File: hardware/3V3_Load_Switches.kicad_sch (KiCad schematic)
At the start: 29 parts, among them Q18 SI2302DDS-T1-GE3, Q19 SI2302DDS-T1-GE3, Q20 SI2302DDS-T1-GE3, U1 LMV321RIYLT, U2 INA199C1DCKR, U3 INA199C1DCKR, U4 INA199C1DCKR, U5 NVTFS5116PLTAG, U6 NVTFS5116PLTAG, U7 NVTFS5116PLTAG

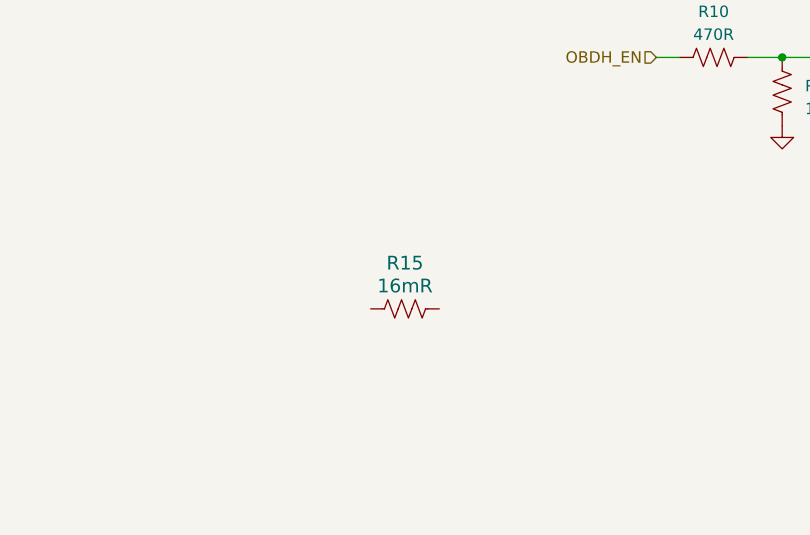
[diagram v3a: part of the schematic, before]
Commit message: hardware: update on footprints
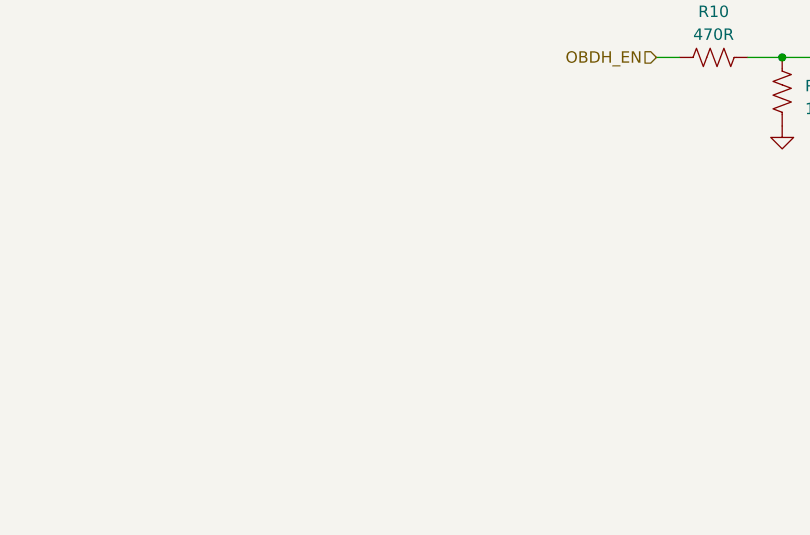
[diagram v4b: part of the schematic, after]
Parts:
- removed R15: 16mR, footprints:WSL2010R0330FEA, symbol WSL2010R0160FEA:WSL2010R0160FEA
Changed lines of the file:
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@@
-    )
-  )
-  (symbol (lib_id "WSL2010R0160FEA:WSL2010R0160FEA") (at 130.81 167.64 0) (unit 1)
-    (in_bom yes) (on_board yes) (dnp no) (fields_autoplaced)
-    (property "Reference" "R15" (at 137.16 162.56 0)
-      (effects (font (size 1.524 1.524)))
-    )
-    (property "Value" "16mR" (at 137.16 165.1 0)
-      (effects (font (size 1.524 1.524)))
-    )
-    (property "Footprint" "footprints:WSL2010R0330FEA" (at 134.62 177.8 0)
-      (effects (font (size 1.27 1.27) italic) hide)
-    )
-    (property "Datasheet" "WSL2010R0330FEA" (at 135.89 175.26 0)
-      (effects (font (size 1.27 1.27) italic) hide)
-    )
-    (pin "1")
-    (pin "2")
-    (instances
-      (project "eps-re_project"
-        (path "/2eebaa11-d7ed-4bfd-bc8e-988f68654d29/b2d6a676-b7d9-423e-8a54-05279452700b"
-          (reference "R15") (unit 1)
-        )
-      )
     )
   )

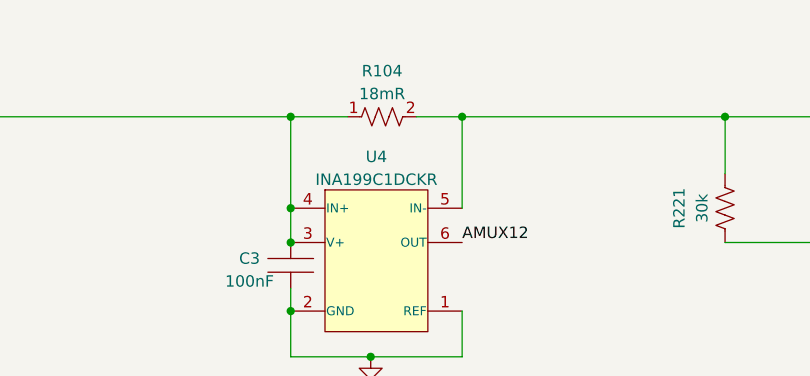
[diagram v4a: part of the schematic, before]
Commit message: hardware: all the resistors were validated, it is only missing the footprint and symbol of one MOSFET and other 4 components which i coulnd't found in the original project.
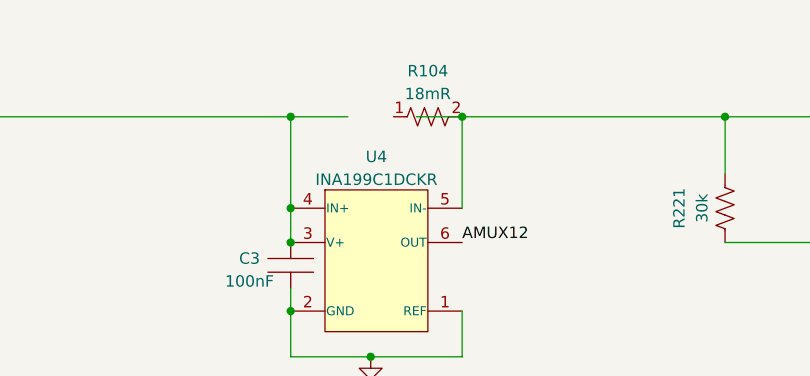
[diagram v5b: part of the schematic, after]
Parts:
- R104: footprint RESC5125X89N -> footprints:WSL2010R0180FEA
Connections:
- net +3V3: no longer R104.1
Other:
- moved on the sheet: R104
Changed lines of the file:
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@@
   (symbol (lib_id "WSL2010R0180FEA:WSL2010R0180FEA") (at 58.42 27.94 0) (unit 1)
     (in_bom yes) (on_board yes) (dnp no) (fields_autoplaced)
-    (property "Reference" "R104" (at 67.31 24.13 0)
-      (effects (font (size 1.27 1.27)))
-    )
-    (property "Value" "18mR" (at 67.31 26.67 0)
-      (effects (font (size 1.27 1.27)))
-    )
-    (property "Footprint" "RESC5125X89N" (at 72.39 124.13 0)
-      (effects (font (size 1.27 1.27)) (justify left top) hide)
-    )
-    (property "Datasheet" "https://www.arrow.com/en/products/wsl2010r0180fea/vishay" (at 72.39 224.13 0)
+    (property "Reference" "R104" (at 72.39 24.13 0)
+      (effects (font (size 1.27 1.27)))
+    )
+    (property "Value" "18mR" (at 72.39 26.67 0)
+      (effects (font (size 1.27 1.27)))
+    )
+    (property "Footprint" "footprints:WSL2010R0180FEA" (at 57.15 31.75 0)
+      (effects (font (size 1.27 1.27)) (justify left top) hide)
+    )
+    (property "Datasheet" "https://www.arrow.com/en/products/wsl2010r0180fea/vishay" (at 44.45 34.29 0)
       (effects (font (size 1.27 1.27)) (justify left top) hide)
     )
@@
       (effects (font (size 1.27 1.27) italic) hide)
     )
-    (property "Datasheet" "https://br.mouser.com/datasheet/2/308/1/NVTFS5116PL_D-2319932.pdf" (at 112.014 31.496 0)
+    (property "Datasheet" "https://br.mouser.com/datasheet/2/308/1/NVTFS5116PL_D-2319932.pdf" (at 111.76 31.75 0)
       (effects (font (size 1.27 1.27) italic) hide)
     )
@@
       (effects (font (size 1.27 1.27) italic) hide)
     )
-    (property "Datasheet" "https://br.mouser.com/datasheet/2/308/1/NVTFS5116PL_D-2319932.pdf" (at 112.014 117.856 0)
+    (property "Datasheet" "https://br.mouser.com/datasheet/2/308/1/NVTFS5116PL_D-2319932.pdf" (at 111.76 118.11 0)
       (effects (font (size 1.27 1.27) italic) hide)
     )
@@
       (effects (font (size 1.27 1.27) italic) hide)
     )
-    (property "Datasheet" "https://br.mouser.com/datasheet/2/308/1/NVTFS5116PL_D-2319932.pdf" (at 110.744 74.676 0)
+    (property "Datasheet" "https://br.mouser.com/datasheet/2/308/1/NVTFS5116PL_D-2319932.pdf" (at 110.49 74.93 0)
       (effects (font (size 1.27 1.27) italic) hide)
     )

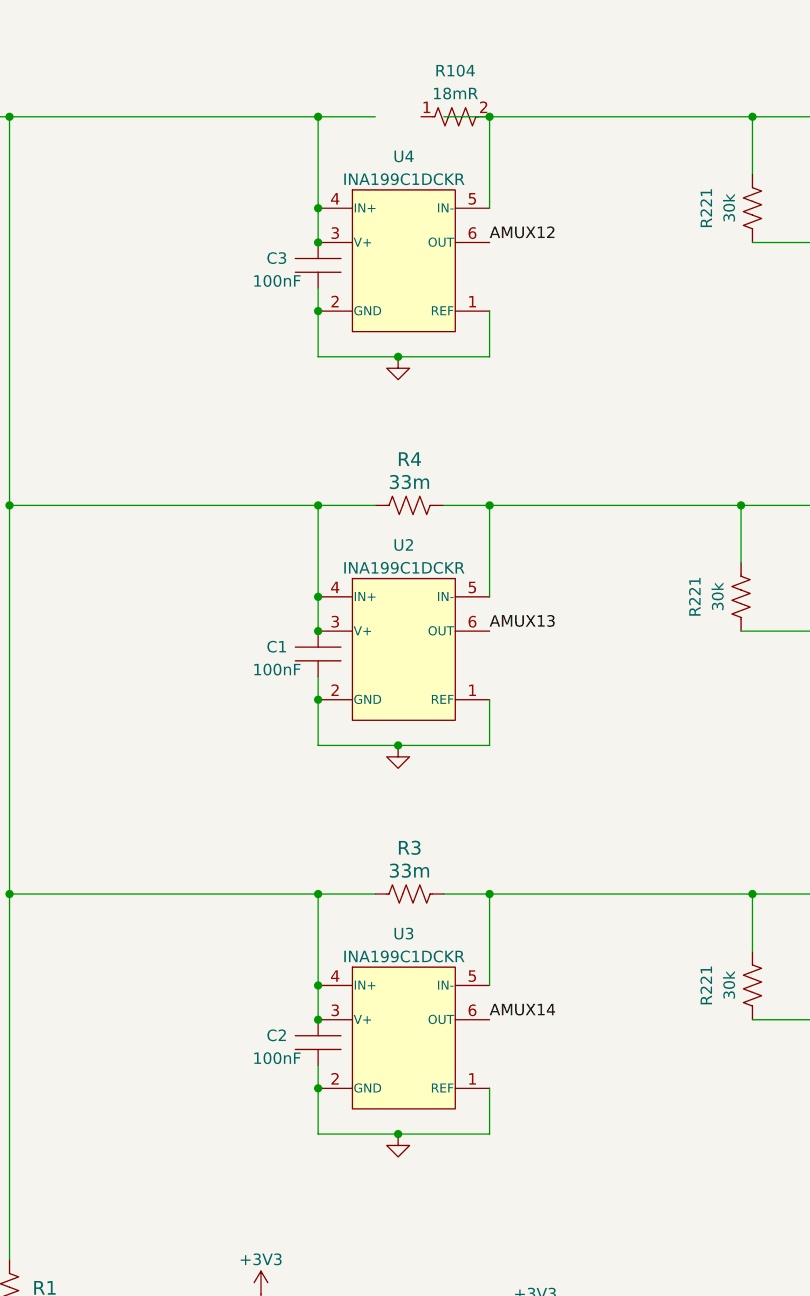
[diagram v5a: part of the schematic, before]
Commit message: hardware: Updating some footprints and 3D models.
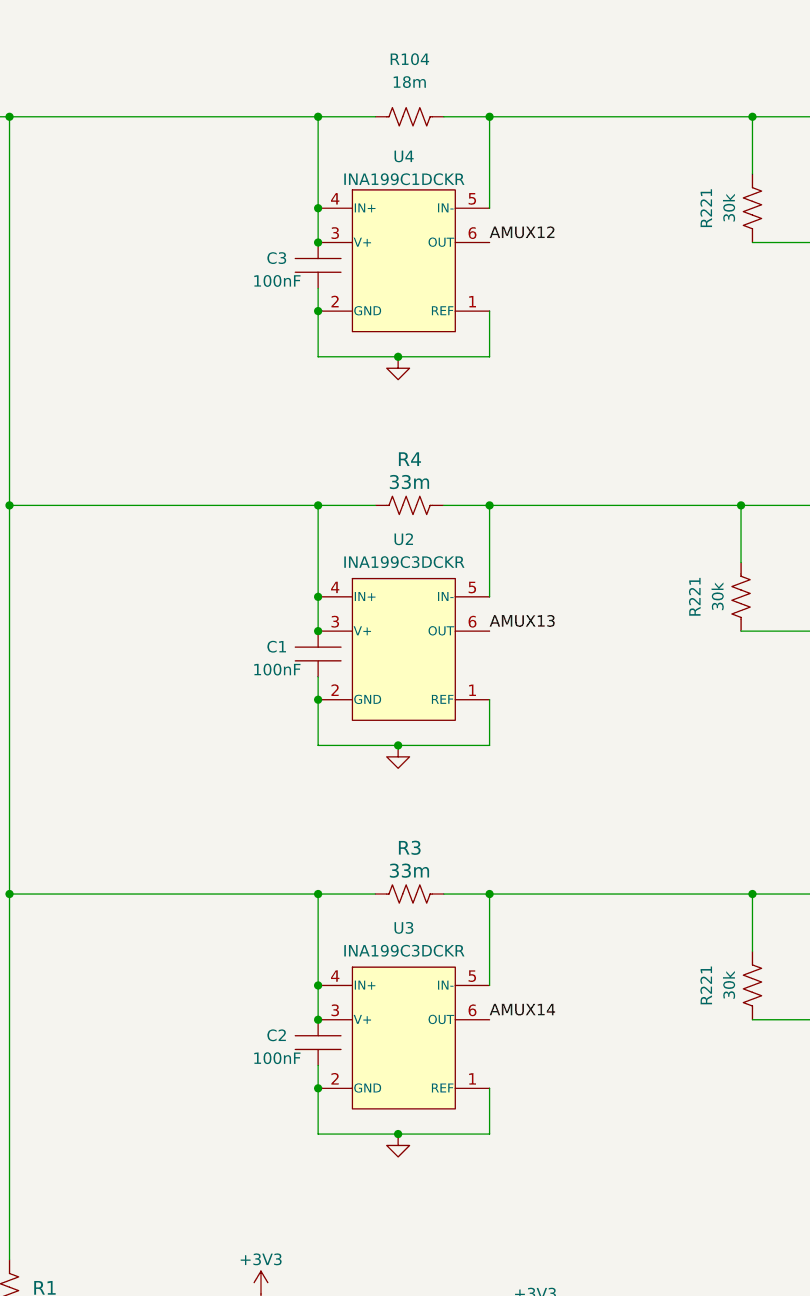
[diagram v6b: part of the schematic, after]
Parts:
- removed U2, U3: INA199C1DCKR, footprints:INA199C1DCKR, symbol INA199C1DCKR:INA199xxDCK
- added U2, U3: INA199C3DCKR, Package_TO_SOT_SMD:SOT-363_SC-70-6, symbol INA199C3DCKR:INA199xxDCK
- R104: value 18mR -> 18m
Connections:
- net +3V3: now also R104.1, U2.3 (V+), U2.4 (IN+), U3.3 (V+), U3.4 (IN+)
- net AMUX13: now also U2.6 (OUT)
- net AMUX14: now also U3.6 (OUT)
- net GND: now also U2.1 (REF), U2.2 (GND), U3.1 (REF), U3.2 (GND)
- net at R221.2, R4.2, U5.1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: now also U2.5 (IN-)
- net at R221.2, R3.2, U6.1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: now also U3.5 (IN-)

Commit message: hardware: Updating 3D models, component placement and more.
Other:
- title: (none) -> Reliability Enhanced Electrical Power System
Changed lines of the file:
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@@
 (kicad_sch (version 20230121) (generator eeschema)
   (paper "A4")
+  (title_block
+    (title "Reliability Enhanced Electrical Power System")
+    (date "2023-08-03")
+    (rev "v0.0")
+    (comment 1 "João C. E. Barcellos <joaoclaudiobarcellos@gmail.com>")
+    (comment 2 "Laura Debastiani <laudebastiani@gmail.com>")
+  )
   (junction (at 133.35 43.18) (diameter 0) (color 0 0 0 0)
   )
